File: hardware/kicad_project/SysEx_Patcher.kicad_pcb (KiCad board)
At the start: 4 copper layers, 172 x 172 mm, 95 parts, among them J1 MIDI_IN, J10 JACK6.35, J2 MIDI_OUT, J3 DC_5V, J4 BAT_PWR, J5 OLED, SW2 SW, SW3 SW, SW4 SW, SW5 SW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

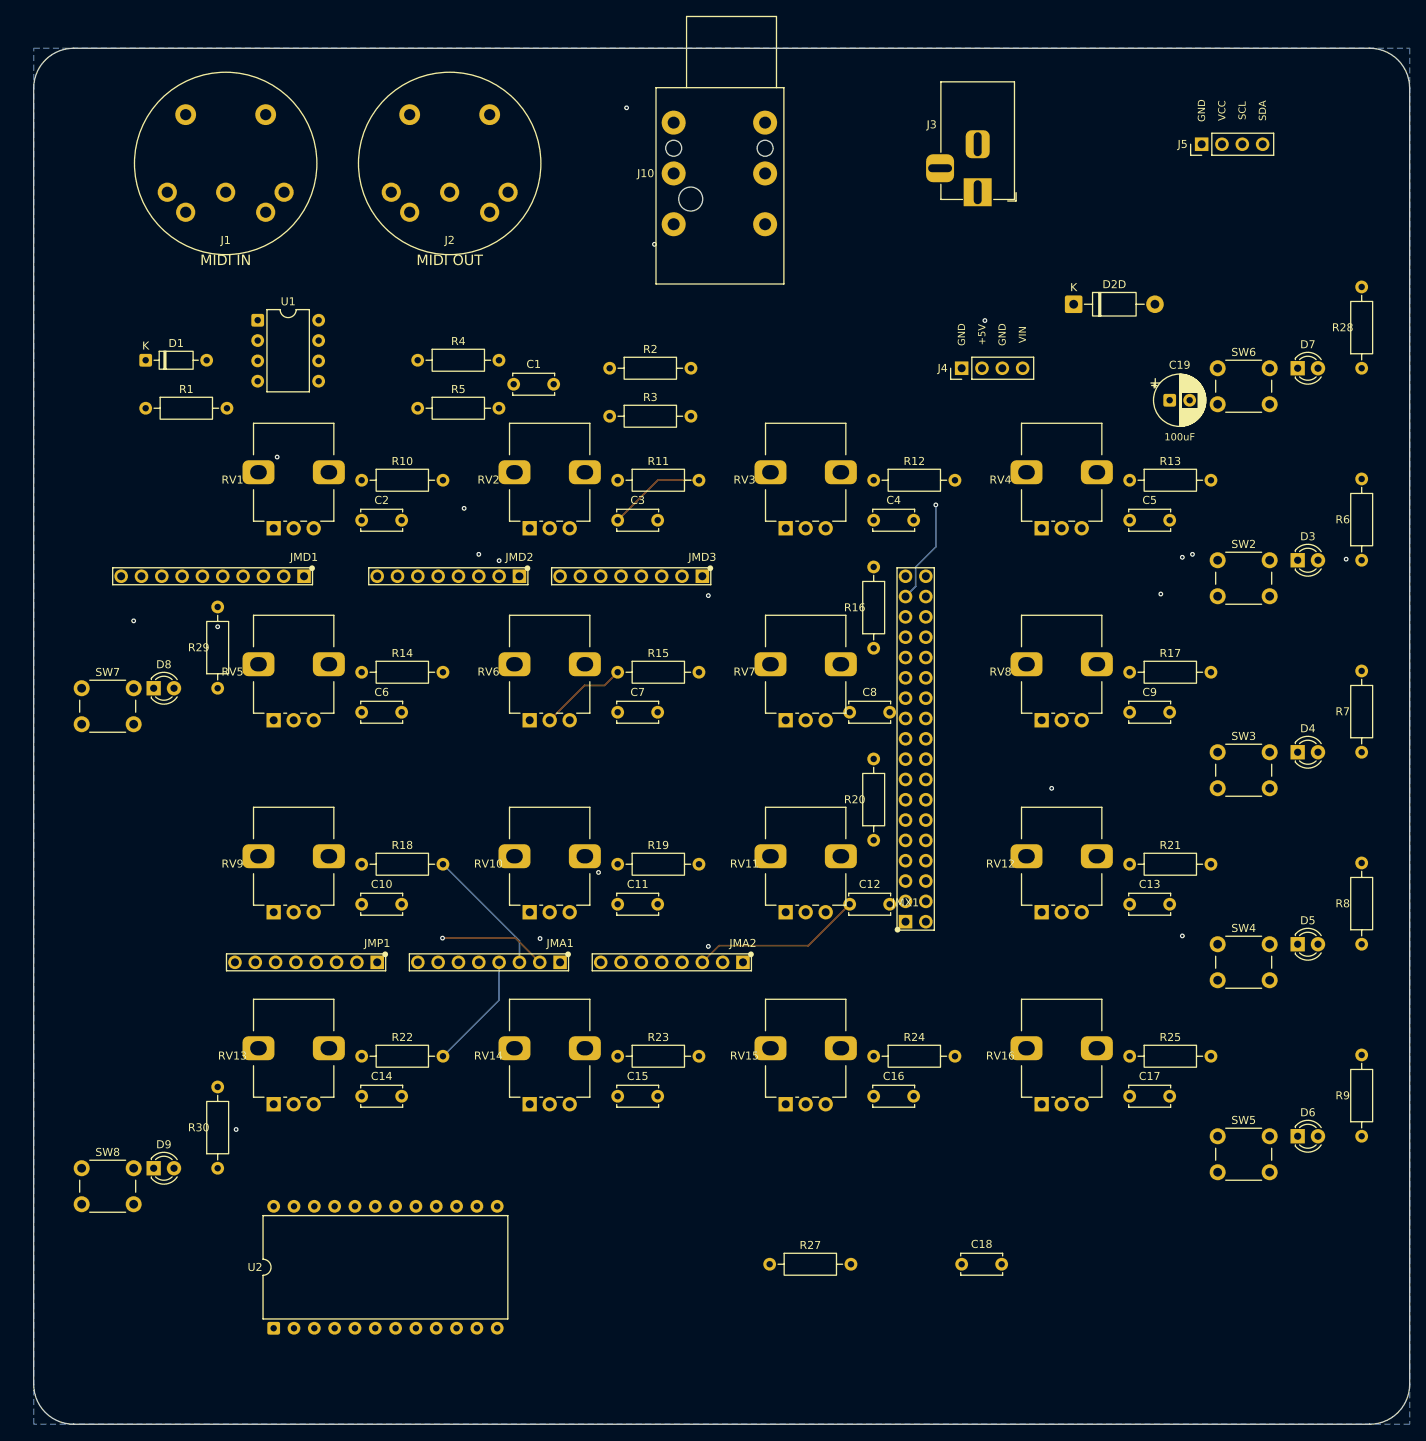
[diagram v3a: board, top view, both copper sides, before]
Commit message: shield: ajout de 4 trous de fixation M3 (3.2mm) aux coins + Gerbers
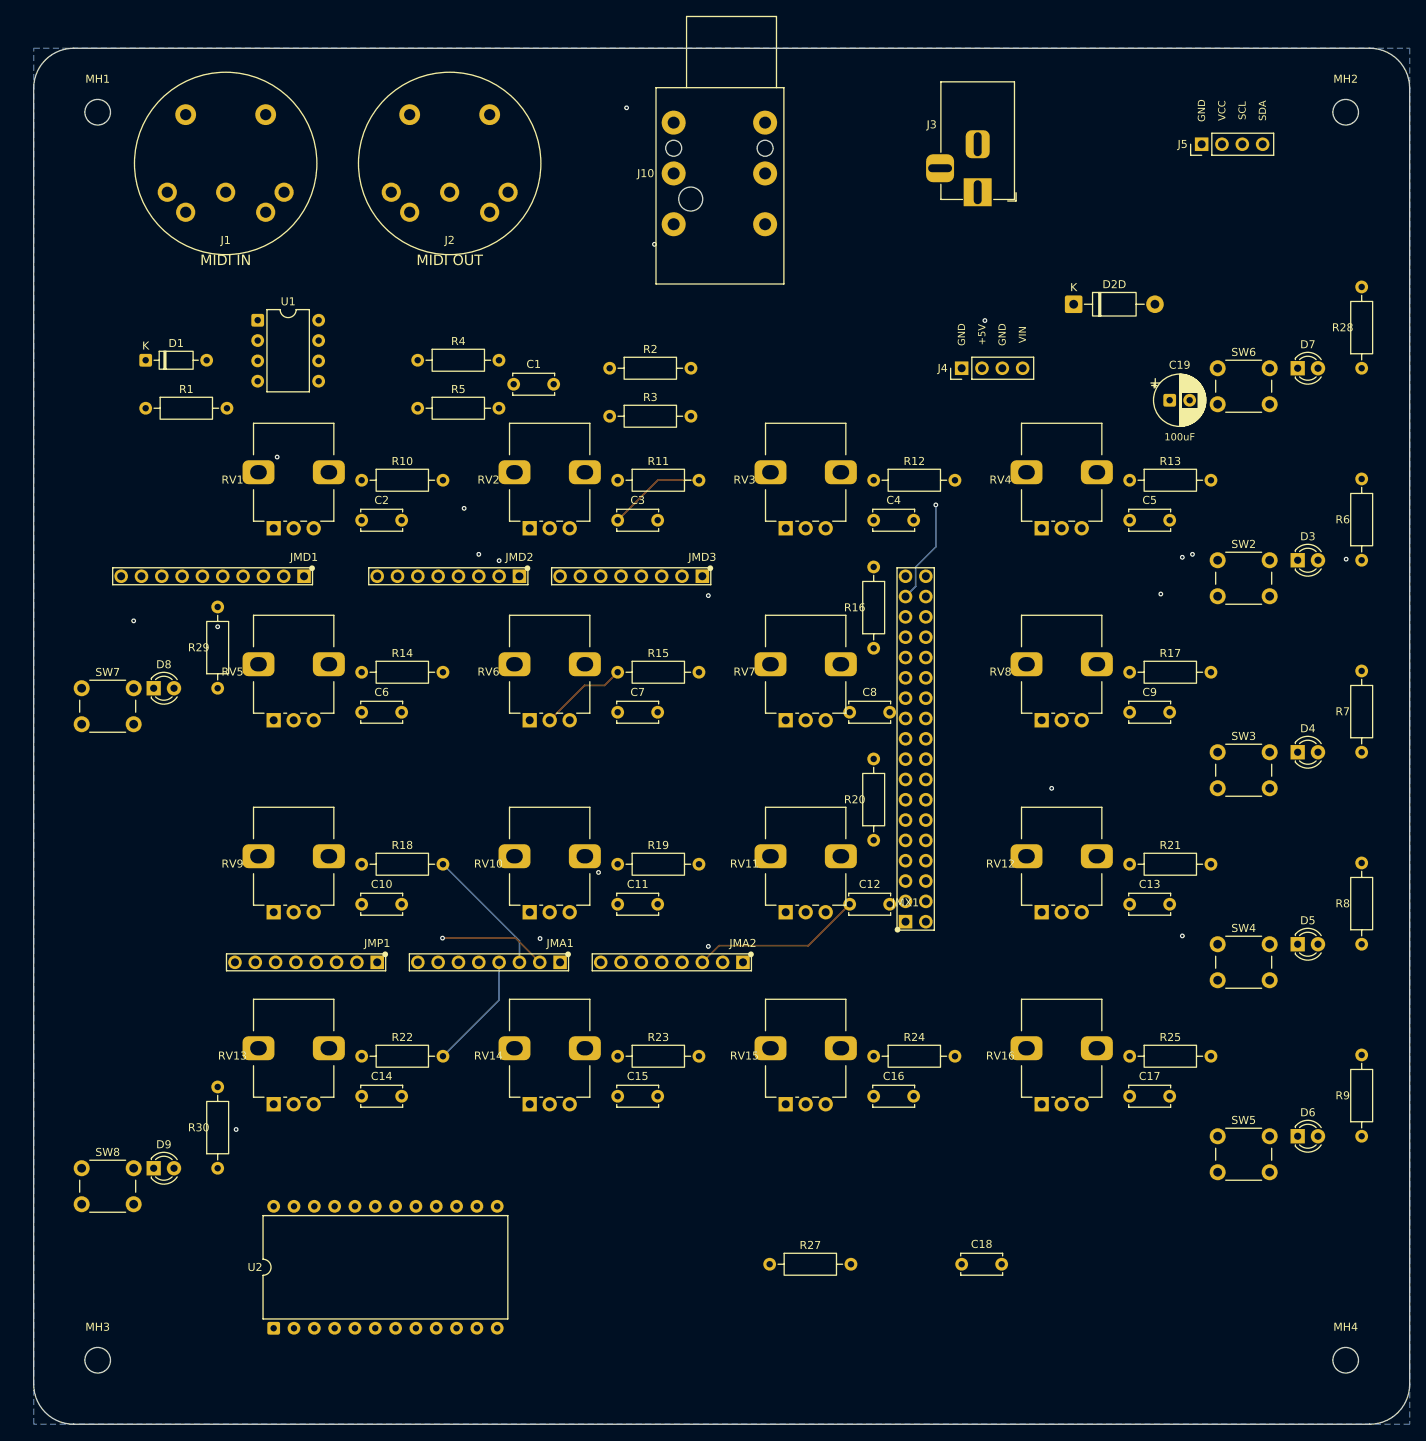
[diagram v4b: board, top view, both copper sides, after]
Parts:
- added MH1: MountingHole_3.2mm_M3, MountingHole:MountingHole_3.2mm_M3, F.Cu at (28.0, 28.0)
- added MH2: MountingHole_3.2mm_M3, MountingHole:MountingHole_3.2mm_M3, F.Cu at (184.0, 28.0)
- added MH3: MountingHole_3.2mm_M3, MountingHole:MountingHole_3.2mm_M3, F.Cu at (28.0, 184.0)
- added MH4: MountingHole_3.2mm_M3, MountingHole:MountingHole_3.2mm_M3, F.Cu at (184.0, 184.0)

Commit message: shield: éloigne C8/C12 des pots et du 2x18 (à droite, vertical) + re-route + Gerbers
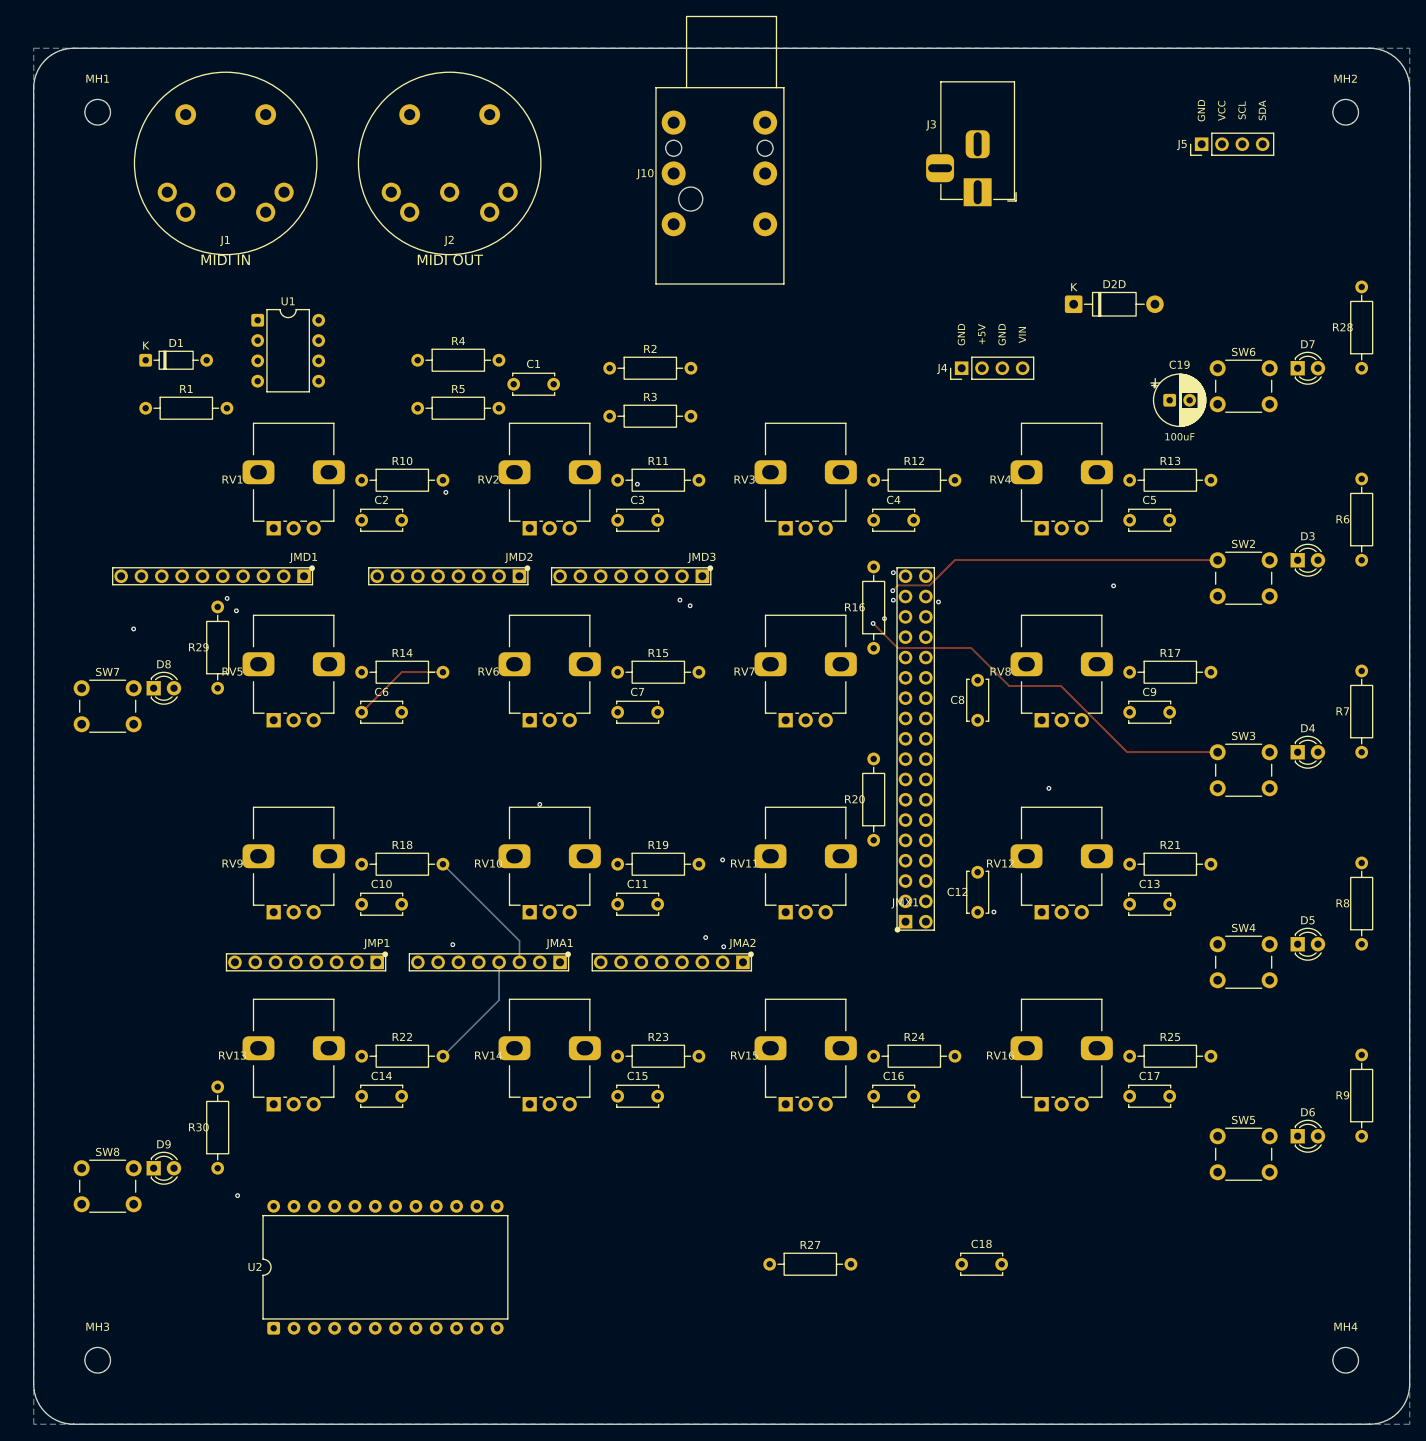
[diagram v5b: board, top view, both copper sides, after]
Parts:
- moved C12 16.0 mm to (138.0, 128.0), turned to 90 degrees
- moved C8 16.0 mm to (138.0, 104.0), turned to 90 degrees
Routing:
- net D21_SCL: track 173.8 -> 142.0 mm
- net D9: track 229.4 -> 207.6 mm, vias 1 -> 2
- net A10: track 40.8 -> 62.6 mm
- net A9: track 57.2 -> 78.0 mm, vias 0 -> 1
- net A0: track 79.2 -> 96.6 mm, vias 0 -> 1
- net D20_SDA: track 164.9 -> 151.4 mm, vias 1 -> 0
- net D3: track 96.3 -> 109.5 mm
- net D10: track 195.8 -> 183.8 mm
- net D5: track 172.9 -> 161.5 mm, vias 2 -> 1
- net A4: track 60.5 -> 50.7 mm, vias 1 -> 0
- net A12: track 107.5 -> 116.3 mm
- net D8: track 160.0 -> 152.9 mm, vias 0 -> 1
- net A7: track 52.2 -> 46.1 mm
- net D13: track 106.6 -> 112.1 mm
- net D6: track 146.5 -> 142.0 mm, vias 3 -> 2
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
